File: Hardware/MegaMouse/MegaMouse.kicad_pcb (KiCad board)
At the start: 2 copper layers, 93.1 x 193 mm, 67 parts, among them J201 Motor, J301 Motor, J401 ICSP, J601 USBC, J602 PROG, SW401 RESET, SW402 START_SW, SW403 STOP/MODE_SW, U101 STATE, U201 DRV8871DDA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

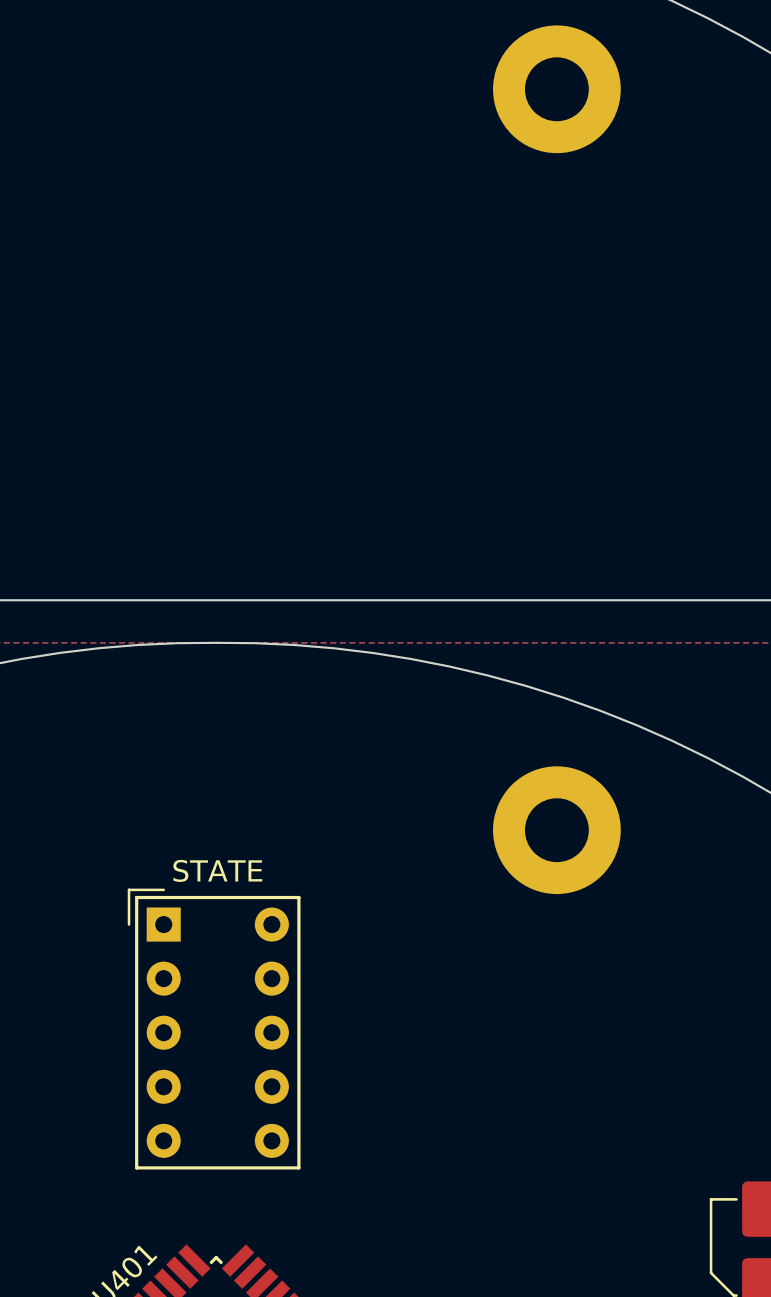
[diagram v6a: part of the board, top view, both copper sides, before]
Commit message: move upper body
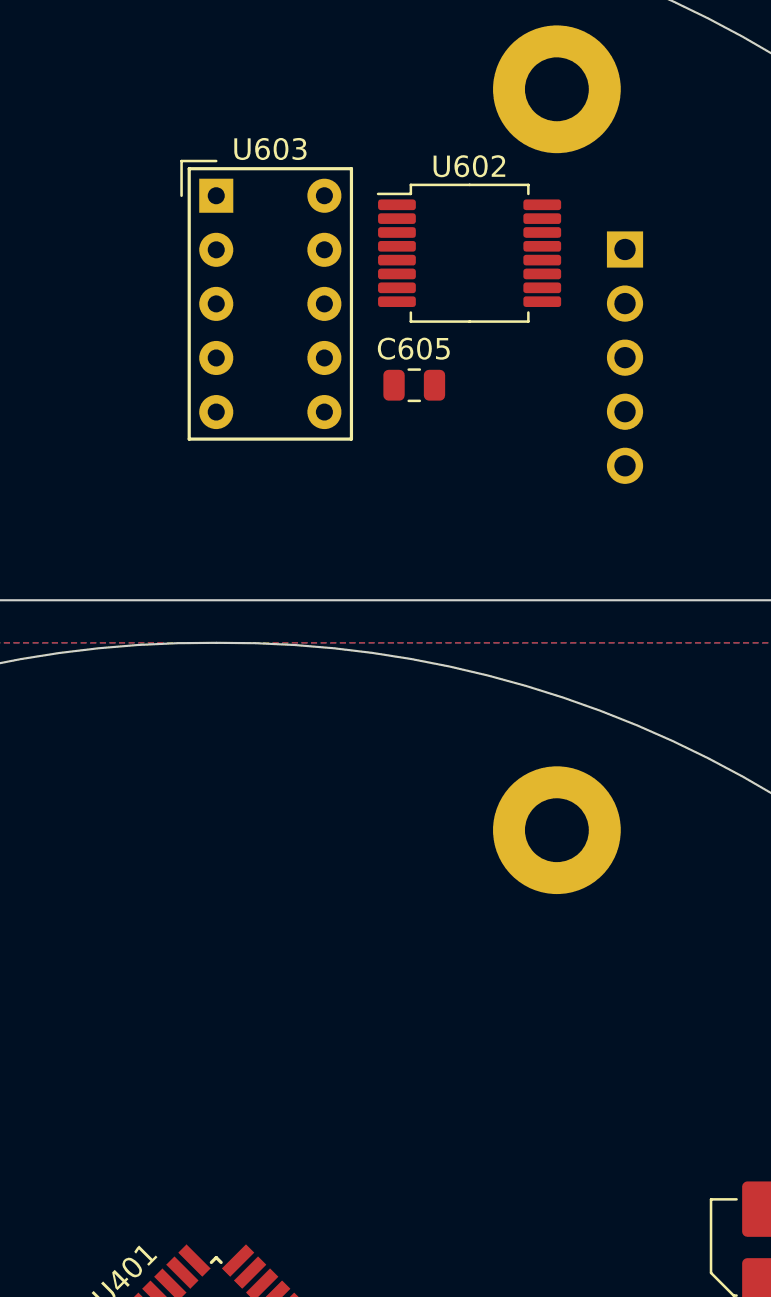
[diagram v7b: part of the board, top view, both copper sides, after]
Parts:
- removed U101: STATE, Display_7Segment:HDSP-7801
- added C605: 100nF, Capacitor_SMD:C_0805_2012Metric, F.Cu at (9.30, -66.1)
- added J603: SHIFT_CONN, Connector_PinHeader_2.54mm:PinHeader_1x05_P2.54mm_Vertical, B.Cu at (19.2, -72.5)
- added U602: SN74HC595, KenwoodFox:SN74HC595, F.Cu at (11.9, -72.3)
- added U603: STATE, Display_7Segment:HDSP-7801, F.Cu at (0.00, -75.0)
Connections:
- net /Programmer/USB+ renamed /Upper Board/USB+
- net /Programmer/USB- renamed /Upper Board/USB-

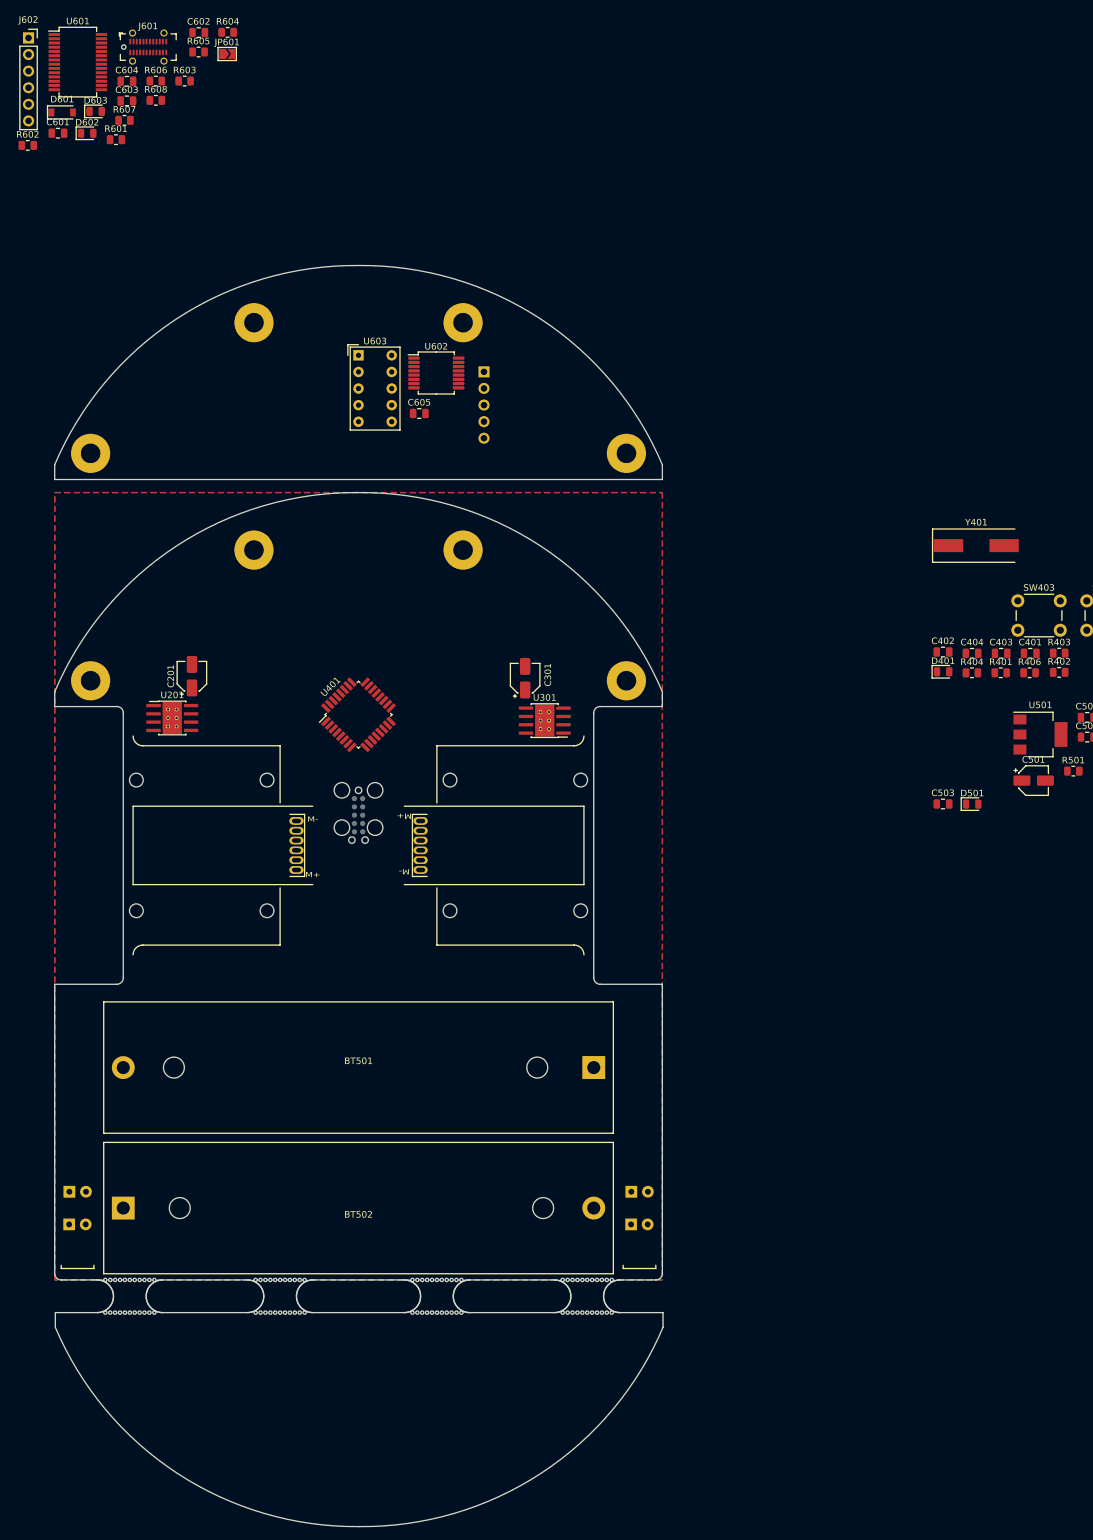
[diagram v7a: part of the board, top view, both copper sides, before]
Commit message: Throw on second layer and target a v1.0
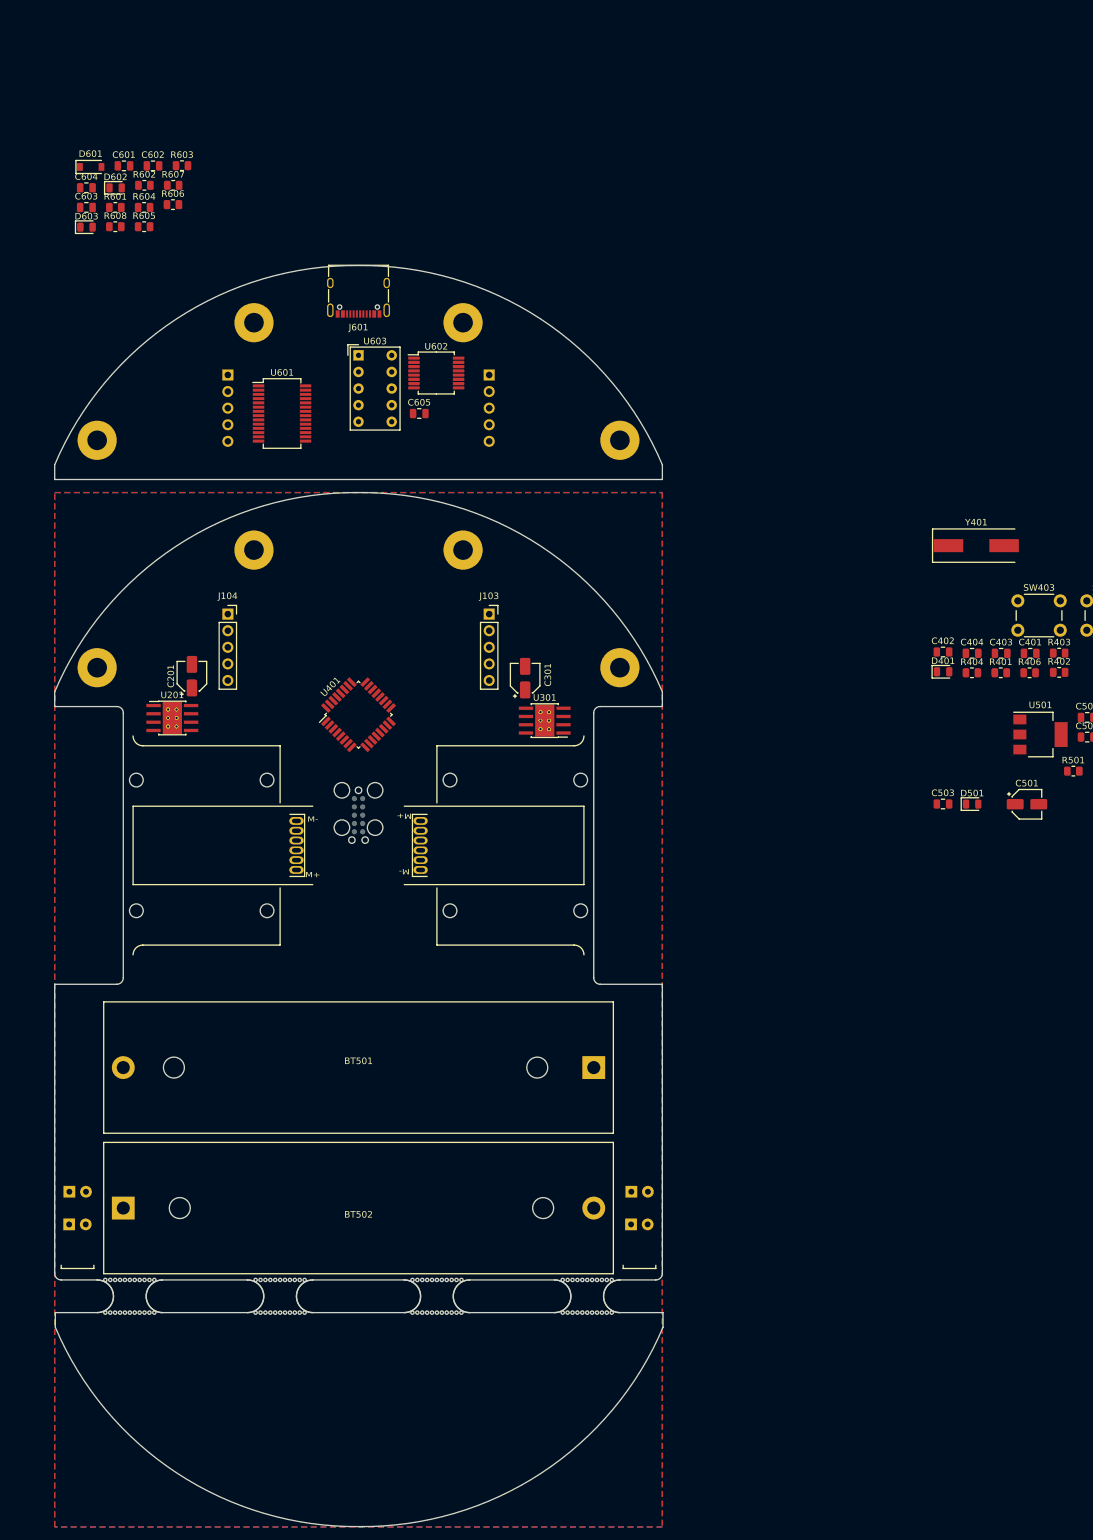
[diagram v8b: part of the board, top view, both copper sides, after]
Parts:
- removed J602: PROG, Connector_PinSocket_2.54mm:PinSocket_1x06_P2.54mm_Vertical
- removed J603: SHIFT_CONN, Connector_PinHeader_2.54mm:PinHeader_1x05_P2.54mm_Vertical
- removed JP601: SolderJumper_2_Open, Jumper:SolderJumper-2_P1.3mm_Open_TrianglePad1.0x1.5mm
- added J101: SHIFT_CONN, Connector_PinHeader_2.54mm:PinHeader_1x05_P2.54mm_Vertical, B.Cu at (20.0, -72.0)
- added J102: PROG_CONN, Connector_PinHeader_2.54mm:PinHeader_1x05_P2.54mm_Vertical, B.Cu at (-20.0, -72.0)
- added J103: SHIFT_CONN, Connector_PinSocket_2.54mm:PinSocket_1x05_P2.54mm_Vertical, F.Cu at (20.0, -35.4)
- added J104: PROG_CONN, Connector_PinSocket_2.54mm:PinSocket_1x05_P2.54mm_Vertical, F.Cu at (-20.0, -35.4)
- J601: footprint Connector_USB:USB_C_Receptacle_GCT_USB4115-03-C -> Connector_USB:USB_C_Receptacle_XKB_U262-16XN-4BVC11
- moved U601 62.2 mm to (-11.7, -66.1)
- moved J601 49.2 mm to (0.00, -85.0), turned to 180 degrees
- moved R604 29.7 mm to (-32.8, -97.6)
- moved R605 28.0 mm to (-32.8, -94.7)
- moved C602 21.6 mm to (-31.4, -104.0)
- moved R608 20.3 mm to (-37.2, -94.7)
- moved R606 19.1 mm to (-28.4, -98.1)
- moved R602 18.9 mm to (-32.8, -101.0)
- moved D603 17.8 mm to (-41.6, -94.6)
- moved C603 17.4 mm to (-41.6, -97.6)
- moved C604 17.4 mm to (-41.6, -100.7)
- moved R603 13.0 mm to (-27.0, -104.0)
- moved R607 12.4 mm to (-28.4, -101.0)
- moved C601 11.3 mm to (-35.9, -104.0)
- moved R601 10.4 mm to (-37.2, -97.6)
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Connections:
- C604 pad 1: /MCU/RST -> /Upper Board/RST
- U601 pad 1: /MCU/RXD -> /Upper Board/TXD
- U601 pad 5: /MCU/TXD -> /Upper Board/RXD
